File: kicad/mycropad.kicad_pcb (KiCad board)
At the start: 2 copper layers, 27 parts, among them SW1 SW_Push, SW2 SW_Push, SW3 SW_Push, SW4 SW_Push, SW5 SW_Push, SW6 SW_Push, SW7 SW_Push, SW8 SW_Push, U1 Pico, U2 SN74AHCT125N

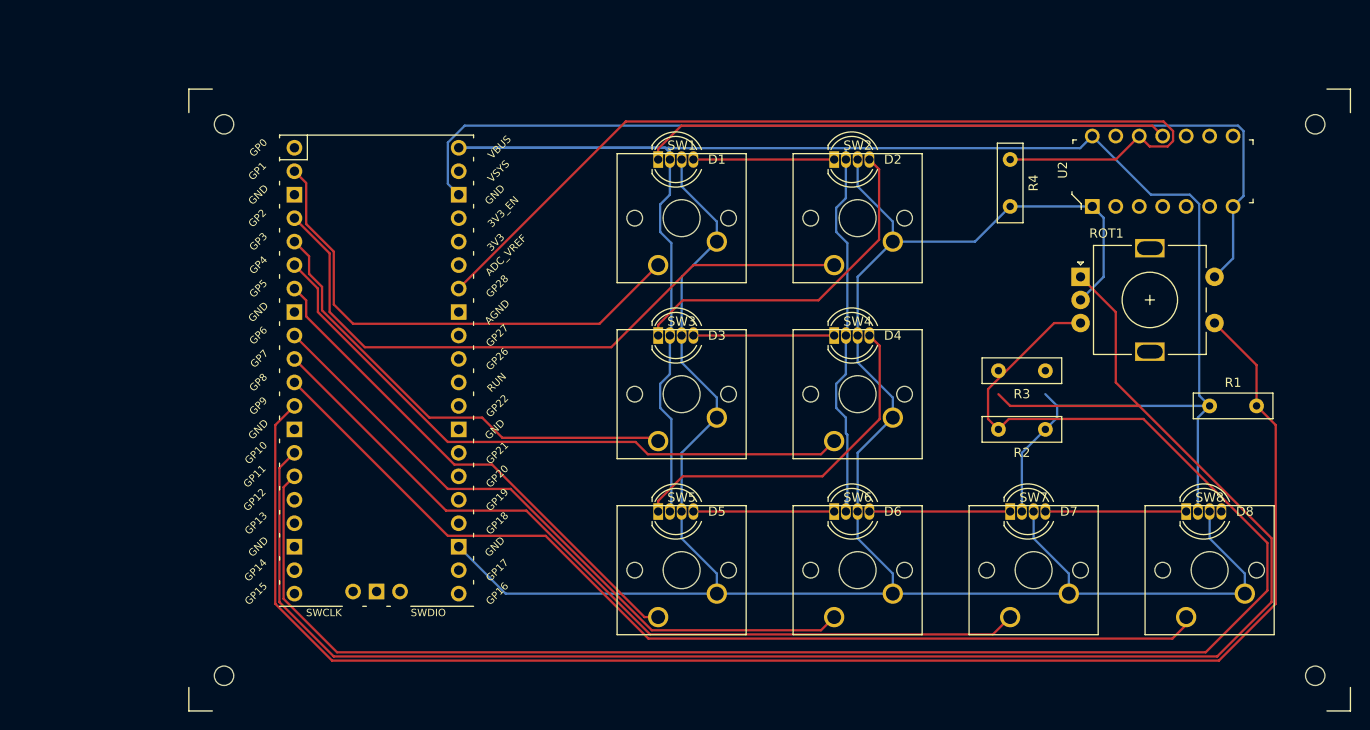
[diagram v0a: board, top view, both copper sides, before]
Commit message: Proper edges given
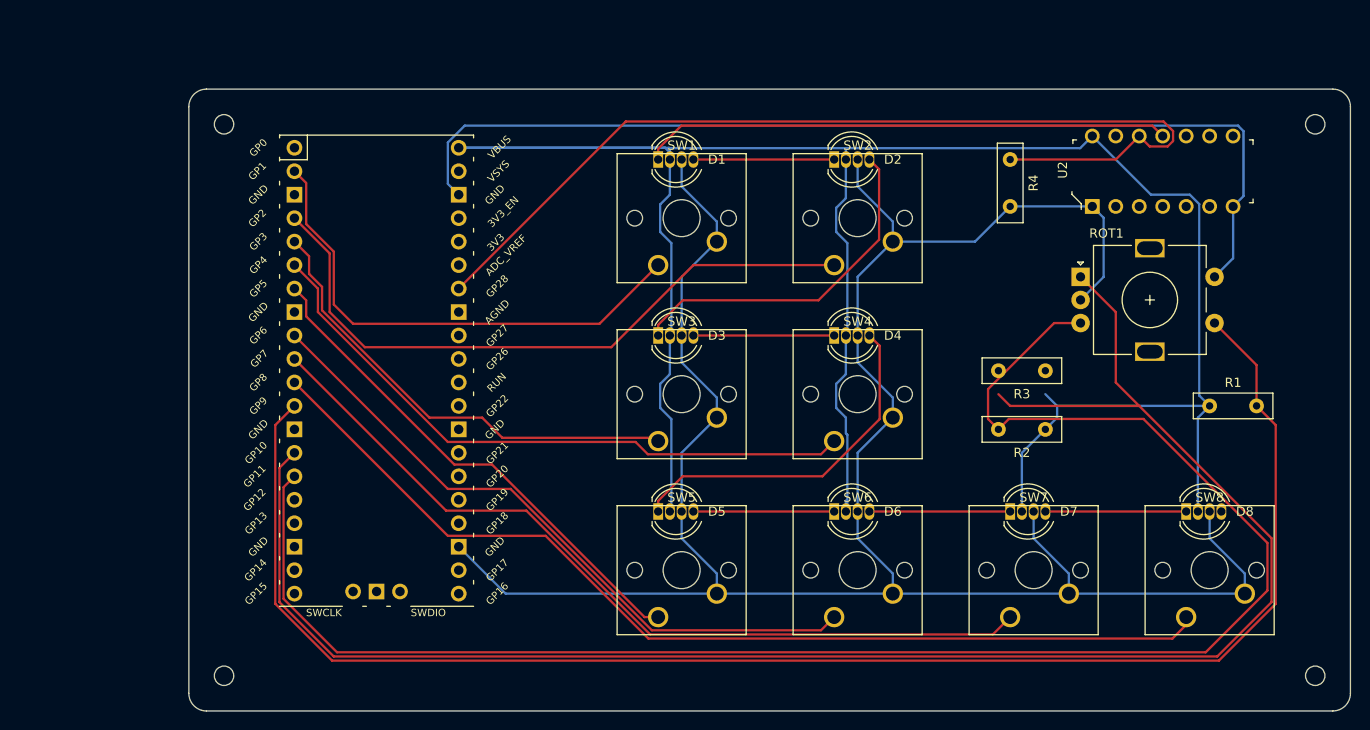
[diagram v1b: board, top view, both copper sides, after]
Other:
- board outline added: 125.7 x 67.3 mm

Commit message: Even better
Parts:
- removed the REF** at (94.0, 134.6)
- removed the REF** at (94.0, 74.9)
- added REF**: MountingHole_2.1mm, MountingHole:MountingHole_2.1mm, F.Cu at (101.0, 134.6)
- added REF**: MountingHole_2.1mm, MountingHole:MountingHole_2.1mm, F.Cu at (101.0, 74.9)
- moved R2 12.5 mm to (177.8, 96.5), turned to 0 degrees
- moved R3 11.4 mm to (177.8, 91.4), turned to 0 degrees
- moved U1 7.01 mm to (117.5, 101.0)
- moved R1 2.29 mm to (199.4, 103.5)
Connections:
- U1 pad 13: Net-(U1-Pad13) -> GND
- U1 pad 18: Net-(U1-Pad18) -> GND
- U1 pad 3: Net-(U1-Pad3) -> GND
- U1 pad 42: Net-(U1-Pad42) -> GND
- U1 pad 8: Net-(U1-Pad8) -> GND
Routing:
- net GND: track 363.1 -> 431.7 mm
- net GPIO18: track 183.5 -> 160.6 mm
- net GPIO17: track 188.6 -> 170.0 mm
- net +5V: track 257.1 -> 247.3 mm
- net GPIO2: track 71.6 -> 64.4 mm
- net GPIO9: track 168.8 -> 162.1 mm
- net GPIO8: track 109.5 -> 102.7 mm
- net GPIO28: track 105.7 -> 99.3 mm
- net GPIO4: track 69.0 -> 62.9 mm
- net GPIO7: track 90.6 -> 84.7 mm
- net GPIO1: track 54.8 -> 49.4 mm
- net GPIO6: track 72.2 -> 67.4 mm
- net GPIO5: track 55.1 -> 51.4 mm
- net GPIO3: track 50.9 -> 47.9 mm
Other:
- board size 125.7 x 67.3 mm -> 118.7 x 67.3 mm
- board text added: "2021-12-25"
- board text added: "designed by meronz"
- board text added: "mycropad v0.1"

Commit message: Added some 3d models
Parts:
- removed the REF** at (212.1, 74.9)
- removed the REF** at (212.1, 134.6)
- removed the REF** at (101.0, 134.6)
- removed the REF** at (101.0, 74.9)
- added REF**: MountingHole_2.2mm_M2_Pad_Via, MountingHole:MountingHole_2.2mm_M2_Pad_Via, F.Cu at (212.1, 74.9)
- added REF**: MountingHole_2.2mm_M2_Pad_Via, MountingHole:MountingHole_2.2mm_M2_Pad_Via, F.Cu at (212.1, 134.6)
- added REF**: MountingHole_2.2mm_M2_Pad_Via, MountingHole:MountingHole_2.2mm_M2_Pad_Via, F.Cu at (101.0, 134.6)
- added REF**: MountingHole_2.2mm_M2_Pad_Via, MountingHole:MountingHole_2.2mm_M2_Pad_Via, F.Cu at (101.0, 74.9)
- SW1, SW2, SW3, SW4, SW5, SW6, SW7, SW8: footprint macropad:SW_Cherry_MX_1.00u_PCB__Rotated -> mycropad:SW_Cherry_MX_1.00u_PCB__Rotated
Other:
- board size 118.7 x 67.3 mm -> 116.2 x 64.8 mm

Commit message: Updated footprints
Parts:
- R1, R2, R3, R4: footprint Resistor_THT:R_Box_L8.4mm_W2.5mm_P5.08mm -> Resistor_THT:R_Axial_DIN0204_L3.6mm_D1.6mm_P5.08mm_Horizontal

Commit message: Moved around some things
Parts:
- moved R4 3.42 mm to (182.2, 77.5)
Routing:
- net GND: track 431.7 -> 414.8 mm
- net GPIO28: track 99.3 -> 86.7 mm
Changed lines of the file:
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@@
     (thickness 1.6)
     (drawings 14)
-    (tracks 259)
+    (tracks 257)
     (zones 0)
     (modules 27)
@@
   )
   (module Resistor_THT:R_Axial_DIN0204_L3.6mm_D1.6mm_P5.08mm_Horizontal (layer F.Cu)
-    (at 179.07 78.74 270)
+    (at 182.245 77.47 270)
     (descr "Resistor, Axial_DIN0204 series, Axial, Horizontal, pin pitch=5.08mm, 0.167W, length*diameter=3.6*1.6mm^2, http://cdn-reichelt.de/documents/datenblatt/B400/1_4W%23YAG.pdf")
     (tags "Resistor Axial_DIN0204 series Axial Horizontal pin pitch 5.08mm 0.167W length 3.6mm diameter 1.6mm")
-    (fp_text reference R4 (at 2.54 -1.92 90) (layer F.SilkS)
+    (fp_text reference R4 (at 2.54 1.905 90) (layer F.SilkS)
       (effects (font (size 1 1) (thickness 0.15)))
     )
@@
   (module digikey-footprints:DIP-14_W3mm (layer F.Cu)
     (at 187.96 83.82 90)
-    (fp_text reference U2 (at 3.94 -3.2 90) (layer F.SilkS)
+    (fp_text reference U2 (at 3.94 -2.54 90) (layer F.SilkS)
       (effects (font (size 1 1) (thickness 0.15)))
     )
@@
   (segment (start 199.534999 103.360001) (end 199.39 103.505) (width 0.25) (layer B.Cu) (net 2))
   (segment (start 199.534999 83.569997) (end 199.534999 103.360001) (width 0.25) (layer B.Cu) (net 2))
-  (segment (start 195.58 76.2) (end 194.454999 75.074999) (width 0.25) (layer F.Cu) (net 3))
-  (segment (start 194.454999 75.074999) (end 143.485001 75.074999) (width 0.25) (layer F.Cu) (net 3))
+  (segment (start 193.284999 78.495001) (end 170.570001 78.495001) (width 0.25) (layer F.Cu) (net 3))
+  (segment (start 195.58 76.2) (end 193.284999 78.495001) (width 0.25) (layer F.Cu) (net 3))
   (segment (start 140.97 77.59) (end 140.97 78.74) (width 0.25) (layer F.Cu) (net 3))
-  (segment (start 143.485001 75.074999) (end 140.97 77.59) (width 0.25) (layer F.Cu) (net 3))
+  (segment (start 141.725 76.835) (end 140.97 77.59) (width 0.25) (layer F.Cu) (net 3))
+  (segment (start 168.91 76.835) (end 141.725 76.835) (width 0.25) (layer F.Cu) (net 3))
+  (segment (start 170.570001 78.495001) (end 168.91 76.835) (width 0.25) (layer F.Cu) (net 3))
   (segment (start 164.885001 87.414001) (end 158.319002 93.98) (width 0.25) (layer F.Cu) (net 4))
   (segment (start 164.885001 79.795001) (end 164.885001 87.414001) (width 0.25) (layer F.Cu) (net 4))
@@
   (segment (start 189.19 85.05) (end 187.96 83.82) (width 0.25) (layer B.Cu) (net 7))
   (segment (start 189.19 91.44) (end 189.19 85.05) (width 0.25) (layer B.Cu) (net 7))
-  (segment (start 187.96 83.82) (end 179.07 83.82) (width 0.25) (layer B.Cu) (net 7))
   (segment (start 204.325001 82.694999) (end 203.2 83.82) (width 0.25) (layer B.Cu) (net 7))
   (segment (start 203.595002 74.93) (end 204.325001 75.659999) (width 0.25) (layer B.Cu) (net 7))
@@
   (segment (start 125.189999 80.739999) (end 125.189999 76.270999) (width 0.25) (layer B.Cu) (net 7))
   (segment (start 126.365 81.915) (end 125.189999 80.739999) (width 0.25) (layer B.Cu) (net 7))
-  (segment (start 179.07 83.82) (end 175.26 87.63) (width 0.25) (layer B.Cu) (net 7))
-  (segment (start 175.26 87.63) (end 166.37 87.63) (width 0.25) (layer B.Cu) (net 7))
   (segment (start 132.08 125.73) (end 147.32 125.73) (width 0.25) (layer B.Cu) (net 7))
   (segment (start 132.08 125.73) (end 126.365 120.015) (width 0.25) (layer B.Cu) (net 7))
@@
   (segment (start 147.32 85.458998) (end 143.51 81.648998) (width 0.25) (layer B.Cu) (net 7))
   (segment (start 143.51 81.648998) (end 143.51 78.74) (width 0.25) (layer B.Cu) (net 7))
+  (segment (start 186.69 82.55) (end 187.96 83.82) (width 0.25) (layer B.Cu) (net 7))
+  (segment (start 183.515 82.55) (end 186.69 82.55) (width 0.25) (layer B.Cu) (net 7))
+  (segment (start 183.515 82.55) (end 182.245 82.55) (width 0.25) (layer B.Cu) (net 7))
   (segment (start 144.78 116.84) (end 160.02 116.84) (width 0.25) (layer F.Cu) (net 8))
   (segment (start 163.83 116.84) (end 179.07 116.84) (width 0.25) (layer F.Cu) (net 9))
@@
   (segment (start 126.739003 116.110001) (end 127.635 117.005998) (width 0.25) (layer F.Cu) (net 22))
   (segment (start 125.000001 116.110001) (end 126.739003 116.110001) (width 0.25) (layer F.Cu) (net 22))
-  (segment (start 193.04 76.2) (end 190.5 78.74) (width 0.25) (layer F.Cu) (net 53))
-  (segment (start 190.5 78.74) (end 179.07 78.74) (width 0.25) (layer F.Cu) (net 53))
-  (segment (start 195.669992 74.62499) (end 196.705001 75.659999) (width 0.25) (layer F.Cu) (net 53))
-  (segment (start 196.705001 75.659999) (end 196.705001 76.740001) (width 0.25) (layer F.Cu) (net 53))
-  (segment (start 196.705001 76.740001) (end 196.120001 77.325001) (width 0.25) (layer F.Cu) (net 53))
-  (segment (start 194.165001 77.325001) (end 193.04 76.2) (width 0.25) (layer F.Cu) (net 53))
-  (segment (start 196.120001 77.325001) (end 194.165001 77.325001) (width 0.25) (layer F.Cu) (net 53))
-  (segment (start 143.065009 74.624989) (end 143.298601 74.624989) (width 0.25) (layer F.Cu) (net 53))
   (segment (start 127.540001 90.899999) (end 127.540001 90.149997) (width 0.25) (layer F.Cu) (net 53))
   (segment (start 127.540001 90.149997) (end 137.737499 79.952499) (width 0.25) (layer F.Cu) (net 53))
   (segment (start 126.365 92.075) (end 127.540001 90.899999) (width 0.25) (layer F.Cu) (net 53))
+  (segment (start 137.46501 80.224988) (end 137.737499 79.952499) (width 0.25) (layer F.Cu) (net 53))
+  (segment (start 191.464989 74.624989) (end 193.04 76.2) (width 0.25) (layer F.Cu) (net 53))
+  (segment (start 143.065009 74.624989) (end 191.464989 74.624989) (width 0.25) (layer F.Cu) (net 53))
   (segment (start 137.737499 79.952499) (end 143.065009 74.624989) (width 0.25) (layer F.Cu) (net 53))
-  (segment (start 137.46501 80.224988) (end 137.737499 79.952499) (width 0.25) (layer F.Cu) (net 53))
-  (segment (start 143.298601 74.624989) (end 195.669992 74.624989) (width 0.25) (layer F.Cu) (net 53))
+  (segment (start 191.77 77.47) (end 193.04 76.2) (width 0.25) (layer F.Cu) (net 53))
+  (segment (start 183.515 77.47) (end 191.77 77.47) (width 0.25) (layer F.Cu) (net 53))
+  (segment (start 183.515 77.47) (end 182.245 77.47) (width 0.25) (layer F.Cu) (net 53))
 )

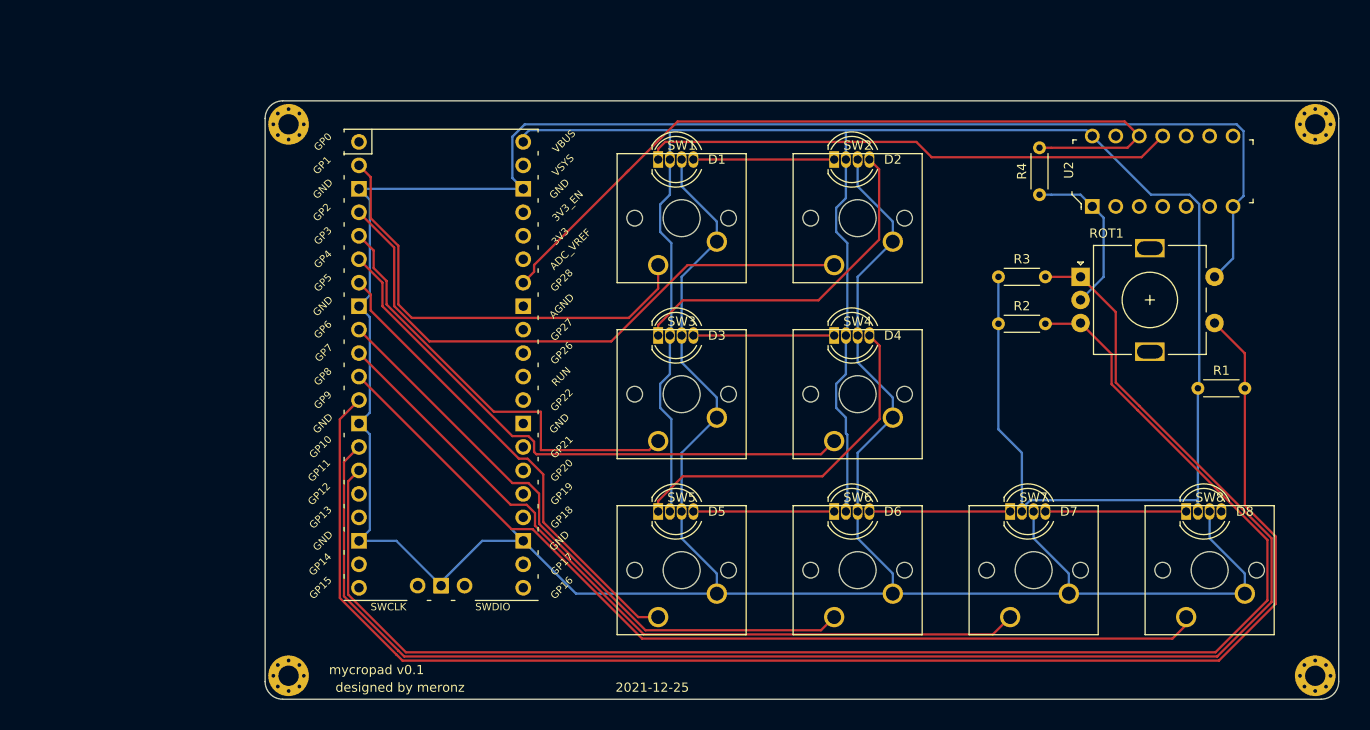
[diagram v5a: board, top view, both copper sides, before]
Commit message: Removed useless resistors, PCB design fixes.
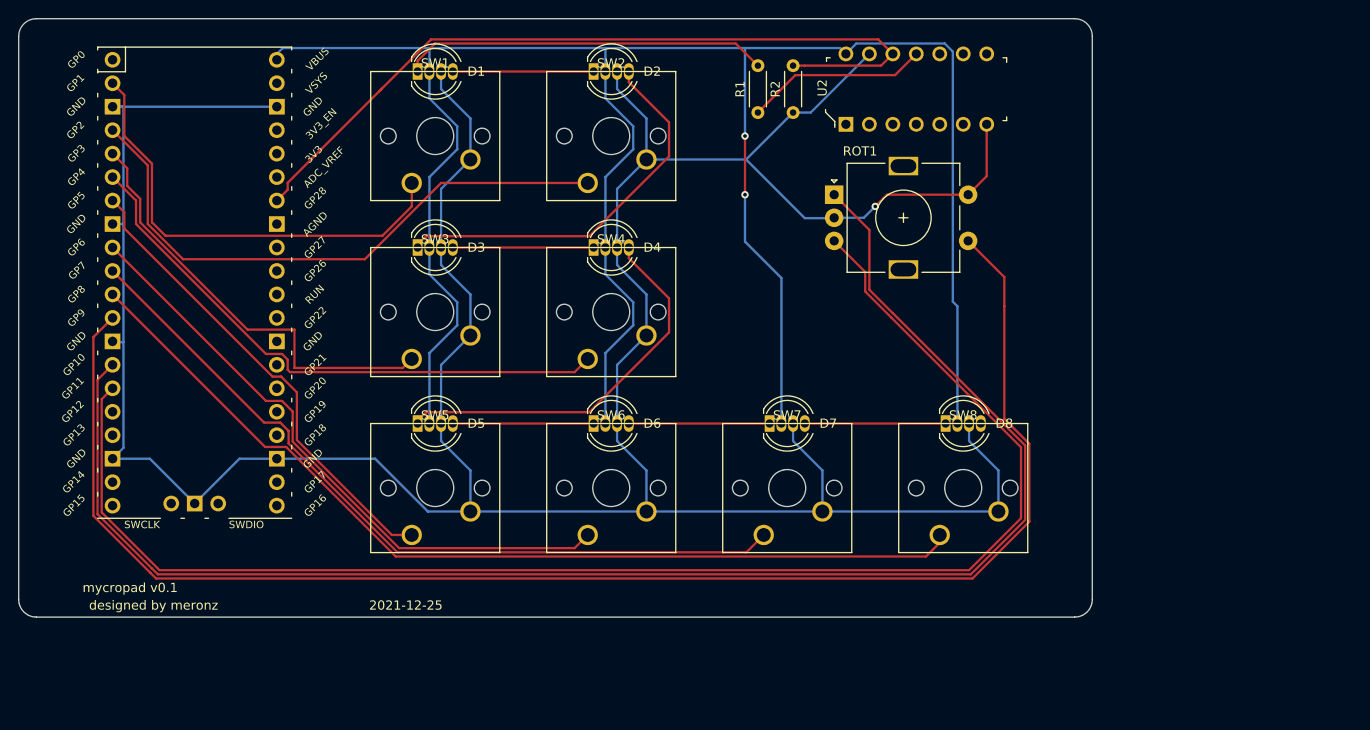
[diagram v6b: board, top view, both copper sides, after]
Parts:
- removed the R2 at (177.8, 96.5)
- removed R3: 10k, Resistor_THT:R_Axial_DIN0204_L3.6mm_D1.6mm_P5.08mm_Horizontal
- removed REF** (x4): MountingHole_2.2mm_M2_Pad_Via, MountingHole:MountingHole_2.2mm_M2_Pad_Via
- R1: value 10k -> 200R
- moved R1 59.1 mm to (151.8, 68.6), turned to 270 degrees
- moved R2 28.1 mm to (155.6, 68.6)
- moved SW1 28.1 mm to (119.4, 71.1)
- moved SW3 28.1 mm to (119.4, 90.2)
- moved SW5 28.1 mm to (119.4, 109.2)
- moved SW7 28.1 mm to (157.5, 109.2)
- moved U2 28.1 mm to (161.3, 74.9)
- moved ROT1 28.1 mm to (160.0, 82.5)
- moved SW2 28.1 mm to (138.4, 71.1)
- moved SW4 28.1 mm to (138.4, 90.2)
- moved SW6 28.1 mm to (138.4, 109.2)
- moved SW8 28.1 mm to (176.5, 109.2)
- moved U1 28.1 mm to (90.8, 92.1)
- moved D3 27.7 mm to (114.9, 88.3)
- moved D4 27.7 mm to (134.0, 88.3)
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- renumbered R4 to R2
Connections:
- D1 pad 1: NEOPIX_5v -> Net-(D1-Pad1)
- R1 pad 1: +5V -> Net-(D1-Pad1)
- R1 pad 2: GPIO9 -> NEOPIX_5v
- U2 pad 1: GND -> Net-(U2-Pad1)
- U2 pad 13: Net-(U2-Pad13) -> GND
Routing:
- net GND: track 414.8 -> 357.3 mm, vias 0 -> 1
- net Net-(D1-Pad1): track 0.00 -> 39.8 mm
- net NEOPIX_5v: track 57.7 -> 19.8 mm
- net Net-(D2-Pad4): track 38.0 -> 42.5 mm
- net Net-(D4-Pad4): track 38.3 -> 42.5 mm
- net GPIO17: track 170.0 -> 166.1 mm
- net GPIO18: track 160.6 -> 156.8 mm
- net +5V: track 247.3 -> 250.6 mm, vias 0 -> 2

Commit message: Restored original RPi SMD footprint
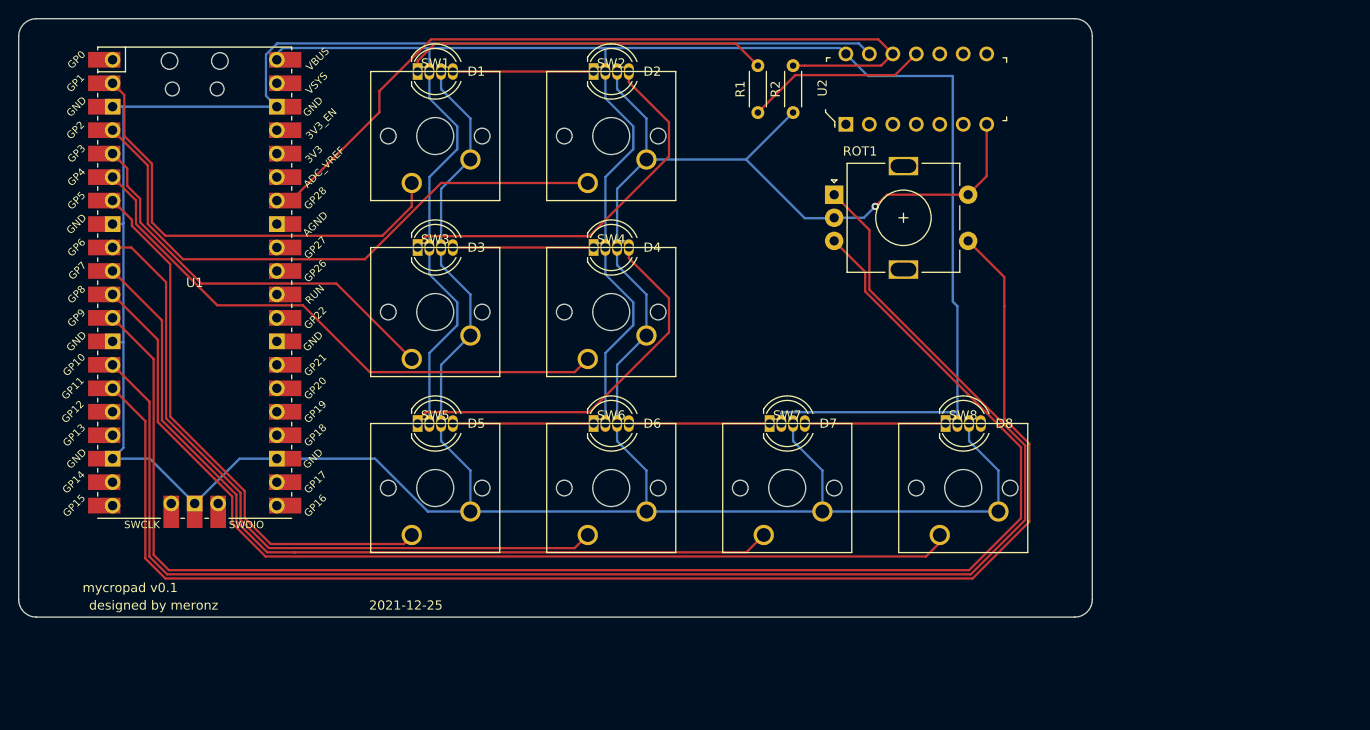
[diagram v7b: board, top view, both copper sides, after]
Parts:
- U1: footprint macropad:RPi_Pico_SMD_TH -> mycropad:RPi_Pico_SMD_TH
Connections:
- net GPIO17 renamed GPIO10
- ROT1 pad B: GPIO18 -> GPIO9
- ROT1 pad S1: GPIO9 -> GPIO11
- U1 pad 15: GPIO18 -> GPIO11
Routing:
- net GPIO18: track 156.8 -> 0.00 mm
- net GPIO11: track 0.00 -> 152.1 mm
- net GND: track 357.3 -> 418.7 mm
- net +5V: track 250.6 -> 227.2 mm, vias 2 -> 0
- net GPIO5: track 51.4 -> 60.0 mm
- net GPIO6: track 67.4 -> 75.8 mm
- net GPIO7: track 84.7 -> 92.1 mm
- net GPIO8: track 102.7 -> 109.7 mm
- net GPIO3: track 47.9 -> 44.2 mm
- net GPIO10: track 166.1 -> 164.2 mm
- net GPIO9: track 162.1 -> 162.9 mm
- net GPIO4: track 62.9 -> 62.3 mm
- net GPIO28: track 86.7 -> 87.2 mm
